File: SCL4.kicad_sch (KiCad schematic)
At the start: 57 parts, among them J1 TSPARE1, J10 8P8C, J2 TSPARE2, J3 Siemens_A1010-A263, J4 TSPARE3, J5 SPARE1, J6 8P8C, J7 5V out, J8 SPARE2, J9 SPARE3, U1 MC3487DX, U2 MC3487DX, U3 TRAM Size 2, U4 MC10H125 (20PLCC), U5 MC10H124 (20PLCC), U6 MC3487DX

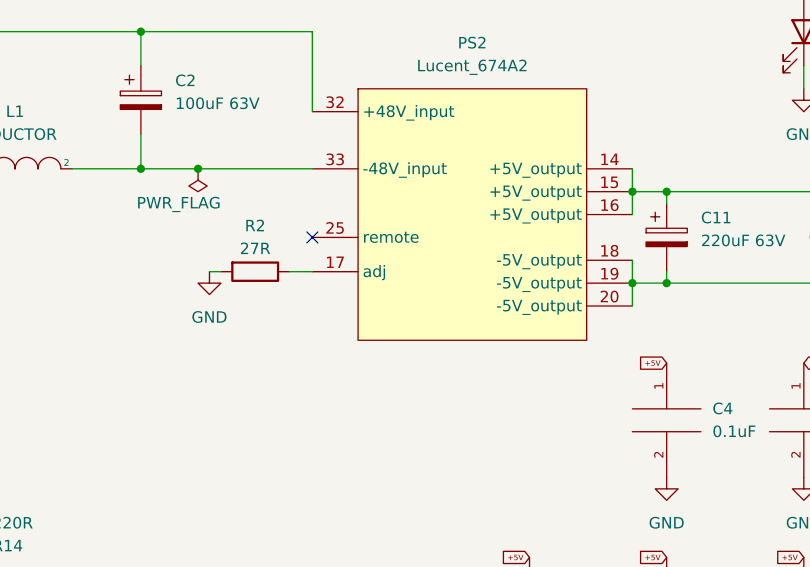
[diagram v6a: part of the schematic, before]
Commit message: fix pins for -5V calibration R
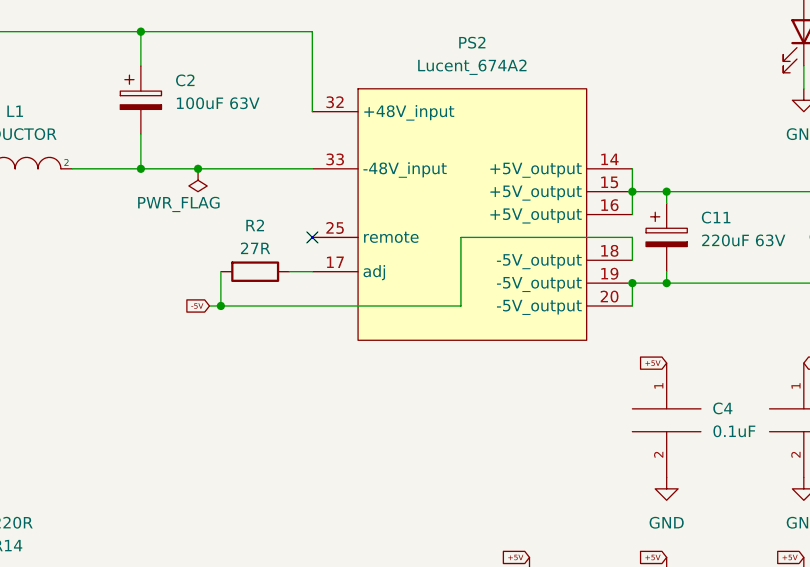
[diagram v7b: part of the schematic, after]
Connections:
- net -5V: now also R2.2
- net GND: no longer R2.2
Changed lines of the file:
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@@
   (junction (at 40.64 154.94) (diameter 0) (color 0 0 0 0)
   )
+  (junction (at 297.18 97.79) (diameter 0) (color 0 0 0 0)
+  )
   (junction (at 259.08 67.31) (diameter 0) (color 0 0 0 0)
   )
@@
     (stroke (width 0) (type default) (color 0 0 0 0))
   )
-  (wire (pts (xy 295.91 93.98) (xy 297.18 93.98))
-    (stroke (width 0) (type default) (color 0 0 0 0))
-  )
   (wire (pts (xy 167.64 82.55) (xy 167.64 81.28))
     (stroke (width 0) (type default) (color 0 0 0 0))
@@
     (stroke (width 0) (type default) (color 0 0 0 0))
   )
+  (wire (pts (xy 297.18 93.98) (xy 297.18 97.79))
+    (stroke (width 0) (type default) (color 0 0 0 0))
+  )
   (wire (pts (xy 107.95 160.02) (xy 106.68 160.02))
     (stroke (width 0) (type default) (color 0 0 0 0))
@@
     (stroke (width 0) (type default) (color 0 0 0 0))
   )
+  (wire (pts (xy 323.85 97.79) (xy 323.85 90.17))
+    (stroke (width 0) (type default) (color 0 0 0 0))
+  )
   (wire (pts (xy 168.91 110.49) (xy 179.07 110.49))
     (stroke (width 0) (type default) (color 0 0 0 0))
@@
     (stroke (width 0) (type default) (color 0 0 0 0))
   )
+  (wire (pts (xy 342.9 90.17) (xy 342.9 92.71))
+    (stroke (width 0) (type default) (color 0 0 0 0))
+  )
   (wire (pts (xy 40.64 152.4) (xy 40.64 154.94))
     (stroke (width 0) (type default) (color 0 0 0 0))
@@
     (stroke (width 0) (type default) (color 0 0 0 0))
   )
+  (wire (pts (xy 323.85 90.17) (xy 342.9 90.17))
+    (stroke (width 0) (type default) (color 0 0 0 0))
+  )
   (wire (pts (xy 288.29 67.31) (xy 307.34 67.31))
     (stroke (width 0) (type default) (color 0 0 0 0))
@@
     (stroke (width 0) (type default) (color 0 0 0 0))
   )
+  (wire (pts (xy 295.91 97.79) (xy 297.18 97.79))
+    (stroke (width 0) (type default) (color 0 0 0 0))
+  )
   (wire (pts (xy 355.6 20.31) (xy 358.14 20.31))
     (stroke (width 0) (type default) (color 0 0 0 0))
@@
     (stroke (width 0) (type default) (color 0 0 0 0))
   )
-  (wire (pts (xy 342.9 92.71) (xy 342.9 95.25))
-    (stroke (width 0) (type default) (color 0 0 0 0))
-  )
   (wire (pts (xy 41.91 231.14) (xy 44.45 231.14))
     (stroke (width 0) (type default) (color 0 0 0 0))
@@
     (stroke (width 0) (type default) (color 0 0 0 0))
   )
+  (wire (pts (xy 297.18 97.79) (xy 323.85 97.79))
+    (stroke (width 0) (type default) (color 0 0 0 0))
+  )
   (wire (pts (xy 213.36 128.27) (xy 231.14 128.27))
     (stroke (width 0) (type default) (color 0 0 0 0))
@@
     )
   )
+  (global_label "-5V" (shape input) (at 295.91 97.79 180) (fields_autoplaced)
+    (effects (font (size 0.6 0.6)) (justify right))
+    (property "Intersheet References" "${INTERSHEET_REFS}" (id 0) (at 292.9414 97.7525 0)
+      (effects (font (size 0.6 0.6)) (justify right) hide)
+    )
+  )
   (global_label "-48V" (shape input) (at 248.92 45.72 180) (fields_autoplaced)
     (effects (font (size 1.27 1.27)) (justify right))
@@
     (pin "1")
   )
-  (symbol (lib_id "power:GND") (at 295.91 93.98 0) (unit 1)
-    (in_bom yes) (on_board yes) (fields_autoplaced)
-    (property "Reference" "#PWR020" (id 0) (at 295.91 100.33 0)
-      (effects (font (size 1.27 1.27)) hide)
-    )
-    (property "Value" "GND" (id 1) (at 295.91 99.06 0))
-    (property "Footprint" "" (id 2) (at 295.91 93.98 0)
-      (effects (font (size 1.27 1.27)) hide)
-    )
-    (property "Datasheet" "" (id 3) (at 295.91 93.98 0)
-      (effects (font (size 1.27 1.27)) hide)
-    )
-    (pin "1")
-  )
   (symbol (lib_id "VI-230-CX:VI-230-CX") (at 320.04 38.1 0) (unit 1)
     (in_bom yes) (on_board yes) (fields_autoplaced)
@@
       (reference "#PWR019") (unit 1) (value "GND") (footprint "")
     )
-    (path "/e41c0d97-a069-4ca5-abd7-f005d9f2146c"
-      (reference "#PWR020") (unit 1) (value "GND") (footprint "")
-    )
     (path "/95d86130-d92b-4faa-b522-02c7d99fb197"
